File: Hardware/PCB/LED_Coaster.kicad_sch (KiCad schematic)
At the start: 88 parts, among them J1 Li-po, J3 USB_C_Receptacle_USB2.0_16P, J4 UART, Q1 AO3401A, SW1 SW_SPDT, U1 ESP32-C3-WROOM-02-H4, U3 MCP73871-2CC, U4 TLV75533PDBVR

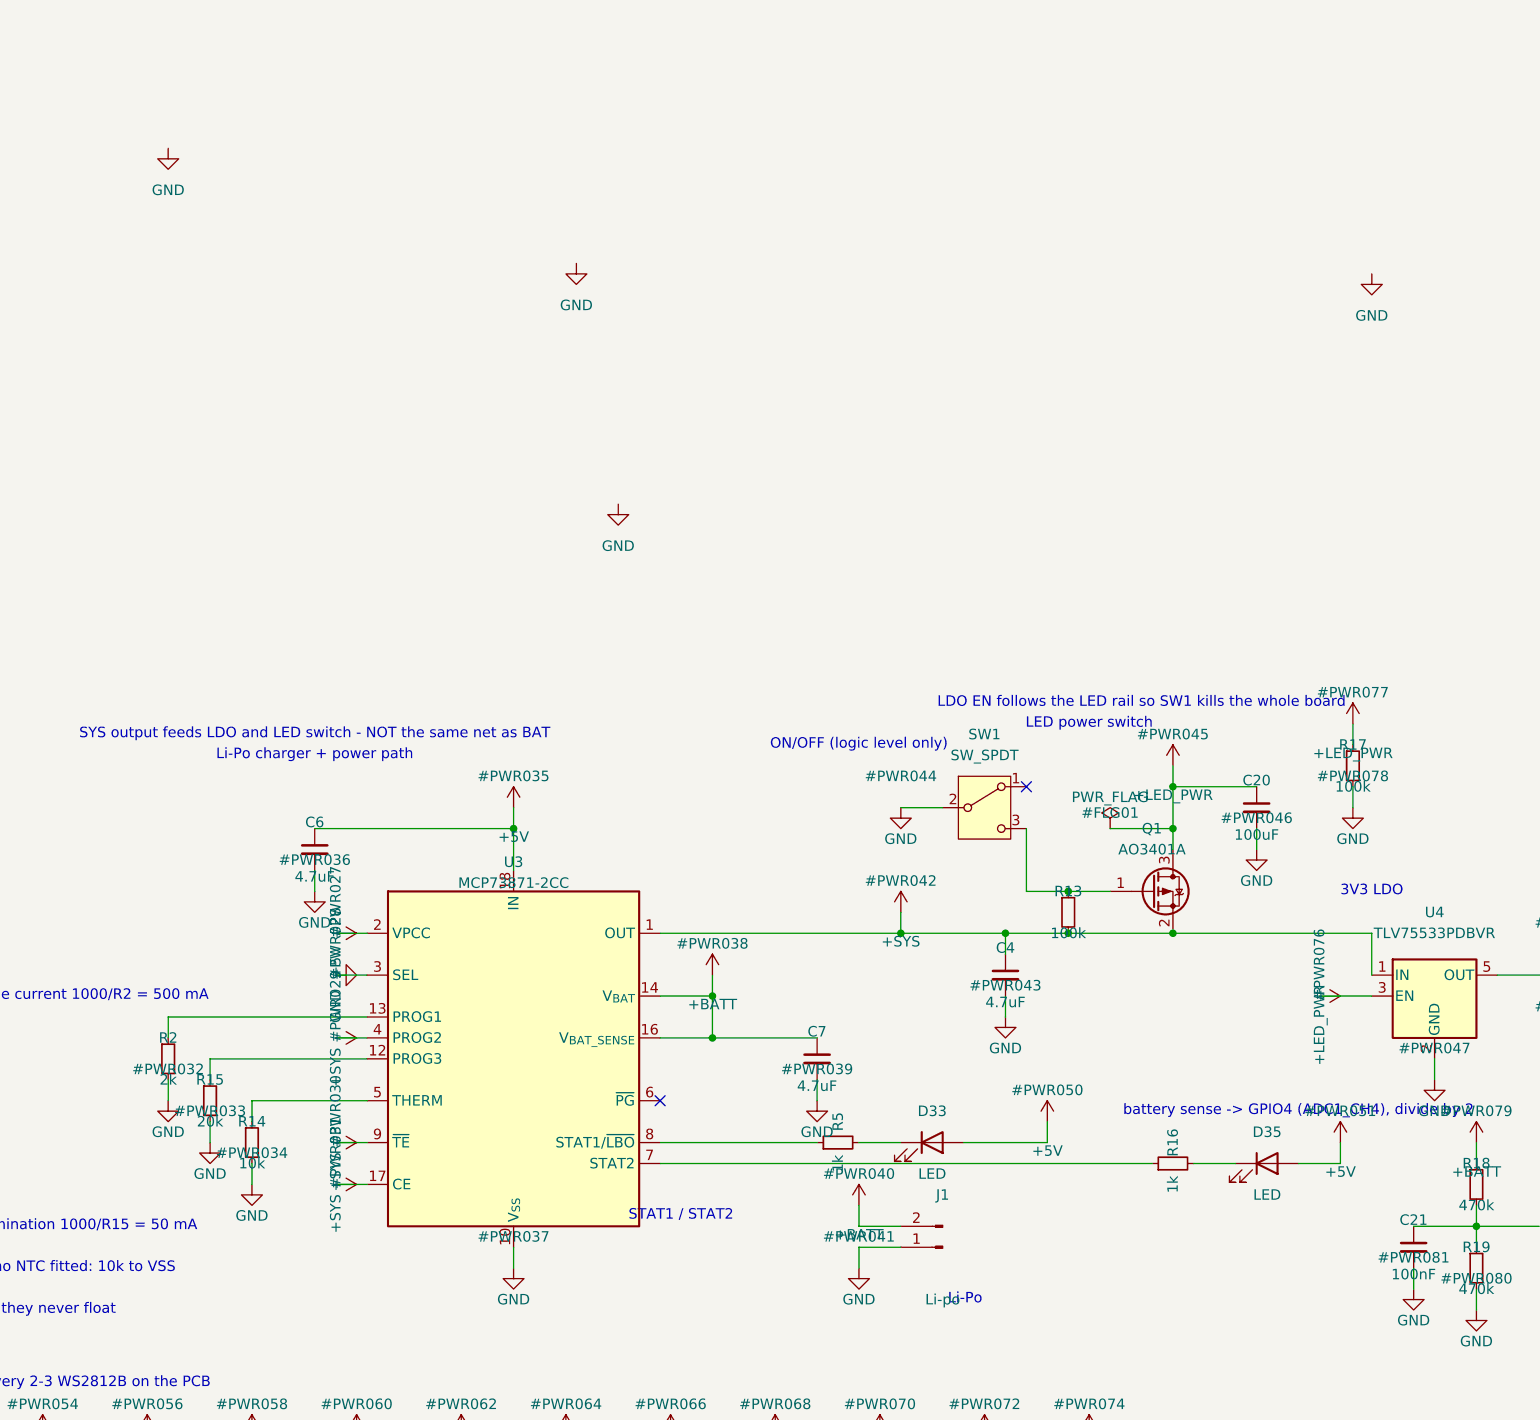
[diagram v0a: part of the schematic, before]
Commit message: Fix ERC errors: remove orphan GND symbols, add PWR_FLAG on +5V and GND
Six ERC errors, from two separate causes.

Four "pin not connected" errors: #PWR05, #PWR09, #PWR011 and #PWR016 were
GND symbols belonging to the old power section that my deletion pass failed
to remove, left floating with nothing attached.

Cause: those four use the GND_1..GND_5 library symbols, whose instances carry
a (lib_name ...) child. That pushes the (at x y rot) line from index 2 to
index 3 of the block, and the region filter read index 2 unconditionally, so
the position never parsed and the symbols were silently kept. 13 symbols in
the file have this shape; 4 of them fell inside the region being cleared.

Two "power pin not driven" errors on +5V (#PWR020) and GND (#PWR02) are
pre-existing, not from the rework. +5V is sourced by the USB-C VBUS pins and
GND by connector and module ground pins, none of which are power_out type, so
ERC has no evidence either rail is driven. Added PWR_FLAG on each, which is
the standard fix. +3V3, +BATT and +SYS were never flagged because the
regulator and charger outputs are real power_out pins, and +LED_PWR already
carries a PWR_FLAG from the earlier commit.

The netlist checker missed the orphans because its unconnected-pin test
skipped any reference starting with #PWR. It now audits every pin regardless
of prefix and reports singleton nets, plus checks that each power symbol
actually lands on a net with other pins on it. Both report clean.

Co-Authored-By: Claude Opus 5 <noreply@anthropic.com>
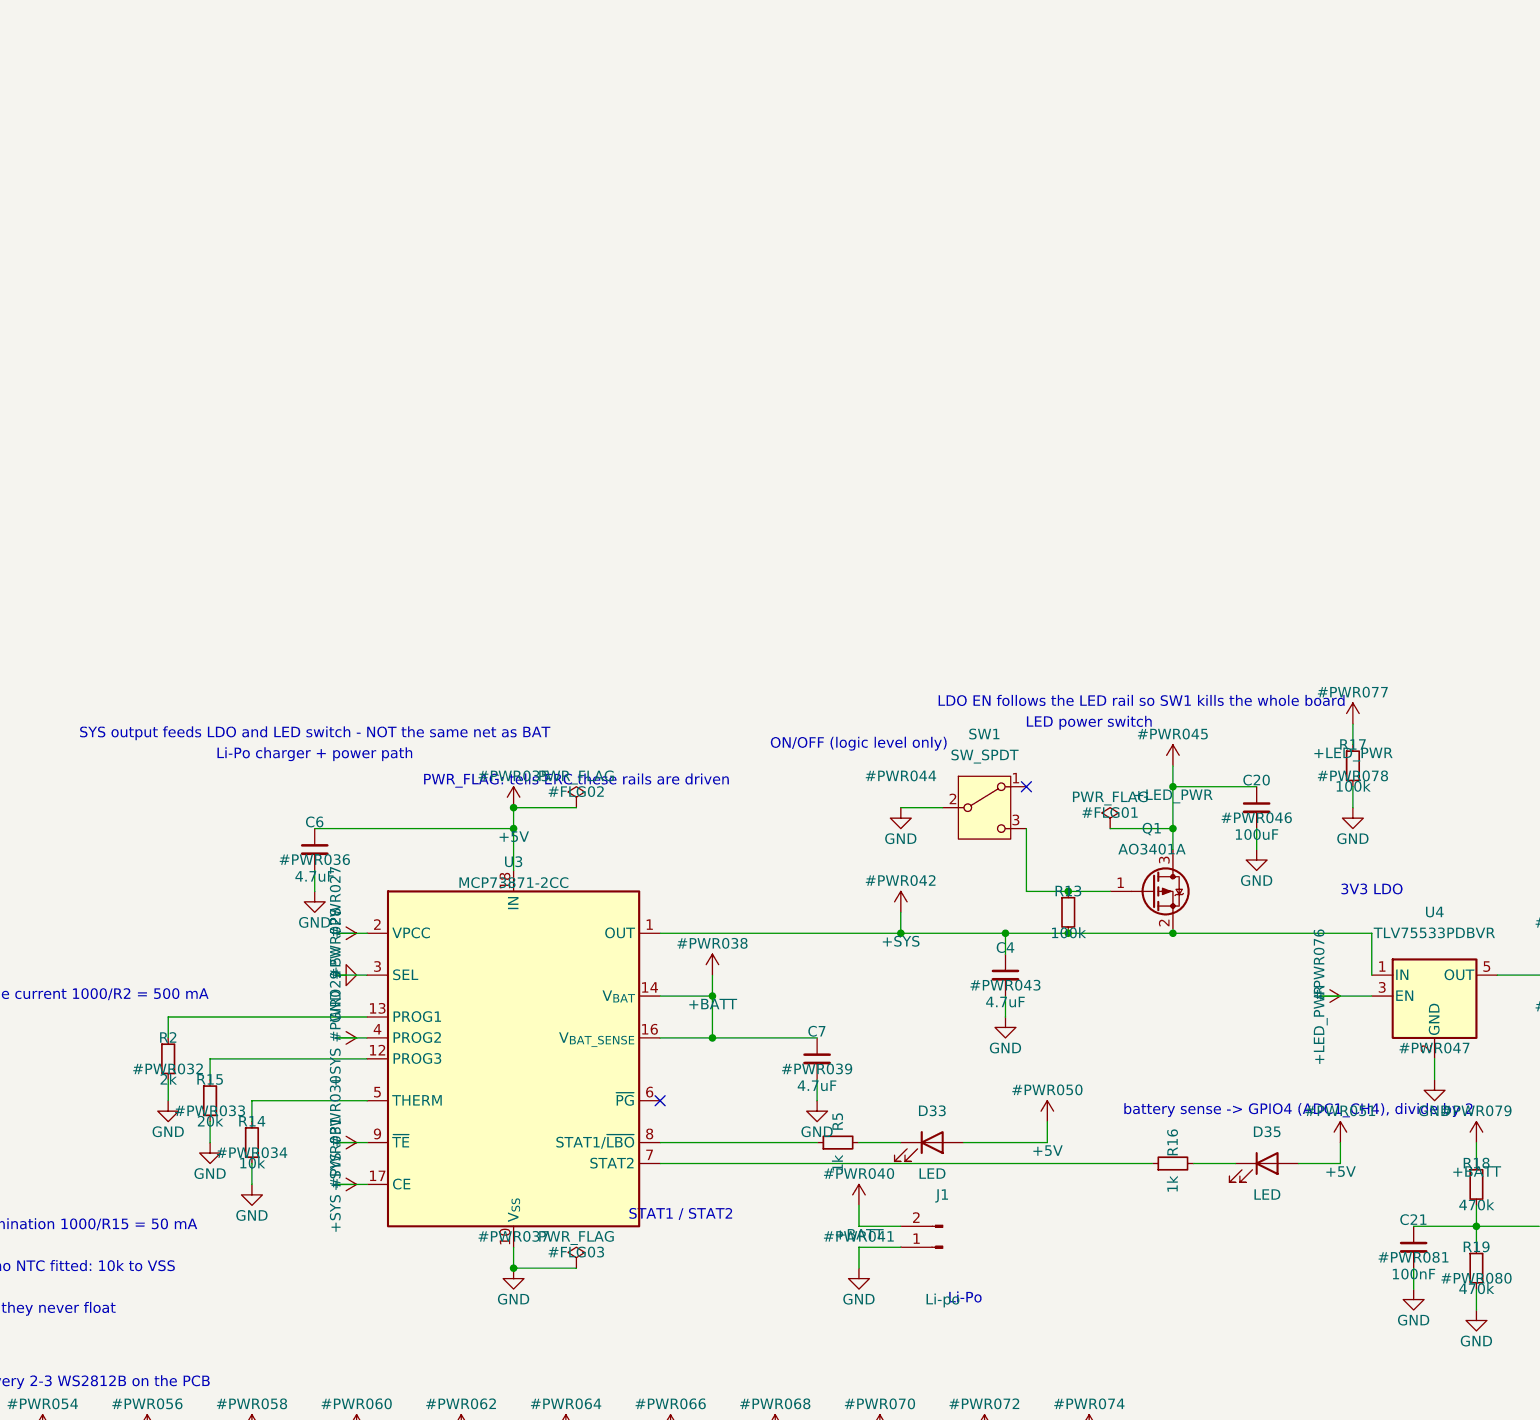
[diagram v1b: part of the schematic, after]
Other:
- note added: "PWR_FLAG: tells ERC these rails are driven"
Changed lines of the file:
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@@
 	)
 	(symbol
-		(lib_name "GND_2")
-		(lib_id "power:GND")
-		(at 422.91 172.72 0)
-		(mirror y)
-		(unit 1)
-		(exclude_from_sim no)
-		(in_bom yes)
-		(on_board yes)
-		(dnp no)
-		(fields_autoplaced yes)
-		(property "Reference" "#PWR016"
-			(at 422.91 179.07 0)
-			(effects
-				(font
-					(size 1.27 1.27)
-				)
-				(hide yes)
-			)
-		)
-		(property "Value" "GND"
-			(at 422.91 177.8 0)
-			(effects
-				(font
-					(size 1.27 1.27)
-				)
-			)
-		)
-		(property "Footprint" ""
-			(at 422.91 172.72 0)
-			(effects
-				(font
-					(size 1.27 1.27)
-				)
-				(hide yes)
-			)
-		)
-		(property "Datasheet" ""
-			(at 422.91 172.72 0)
-			(effects
-				(font
-					(size 1.27 1.27)
-				)
-				(hide yes)
-			)
-		)
-		(property "Description" "Power symbol creates a global label with name \"GND\" , ground"
-			(at 422.91 172.72 0)
-			(effects
-				(font
-					(size 1.27 1.27)
-				)
-				(hide yes)
-			)
-		)
-		(pin "1"
-		)
-		(instances
-			(project "LED_Coaster"
-				(path "/c3ec28d0-7d6a-45c7-8929-905948ef9c11"
-					(reference "#PWR016")
-					(unit 1)
-				)
-			)
-		)
-	)
-	(symbol
 		(lib_id "Switch:SW_SPST")
 		(at 227.33 198.12 0)
@@
 	)
 	(symbol
-		(lib_name "GND_2")
-		(lib_id "power:GND")
-		(at 514.35 144.78 0)
-		(unit 1)
-		(exclude_from_sim no)
-		(in_bom yes)
-		(on_board yes)
-		(dnp no)
-		(fields_autoplaced yes)
-		(property "Reference" "#PWR05"
-			(at 514.35 151.13 0)
-			(effects
-				(font
-					(size 1.27 1.27)
-				)
-				(hide yes)
-			)
-		)
-		(property "Value" "GND"
-			(at 514.35 149.86 0)
-			(effects
-				(font
-					(size 1.27 1.27)
-				)
-			)
-		)
-		(property "Footprint" ""
-			(at 514.35 144.78 0)
-			(effects
-				(font
-					(size 1.27 1.27)
-				)
-				(hide yes)
-			)
-		)
-		(property "Datasheet" ""
-			(at 514.35 144.78 0)
-			(effects
-				(font
-					(size 1.27 1.27)
-				)
-				(hide yes)
-			)
-		)
-		(property "Description" "Power symbol creates a global label with name \"GND\" , ground"
-			(at 514.35 144.78 0)
-			(effects
-				(font
-					(size 1.27 1.27)
-				)
-				(hide yes)
-			)
-		)
-		(pin "1"
-		)
-		(instances
-			(project "LED_Coaster"
-				(path "/c3ec28d0-7d6a-45c7-8929-905948ef9c11"
-					(reference "#PWR05")
-					(unit 1)
-				)
-			)
-		)
-	)
-	(symbol
 		(lib_name "GND_4")
 		(lib_id "power:GND")
@@
 	)
 	(symbol
-		(lib_name "GND_3")
-		(lib_id "power:GND")
-		(at 368.3 129.54 0)
-		(unit 1)
-		(exclude_from_sim no)
-		(in_bom yes)
-		(on_board yes)
-		(dnp no)
-		(fields_autoplaced yes)
-		(property "Reference" "#PWR09"
-			(at 368.3 135.89 0)
-			(effects
-				(font
-					(size 1.27 1.27)
-				)
-				(hide yes)
-			)
-		)
-		(property "Value" "GND"
-			(at 368.3 134.62 0)
-			(effects
-				(font
-					(size 1.27 1.27)
-				)
-			)
-		)
-		(property "Footprint" ""
-			(at 368.3 129.54 0)
-			(effects
-				(font
-					(size 1.27 1.27)
-				)
-				(hide yes)
-			)
-		)
-		(property "Datasheet" ""
-			(at 368.3 129.54 0)
-			(effects
-				(font
-					(size 1.27 1.27)
-				)
-				(hide yes)
-			)
-		)
-		(property "Description" "Power symbol creates a global label with name \"GND\" , ground"
-			(at 368.3 129.54 0)
-			(effects
-				(font
-					(size 1.27 1.27)
-				)
-				(hide yes)
-			)
-		)
-		(pin "1"
-		)
-		(instances
-			(project "LED_Coaster"
-				(path "/c3ec28d0-7d6a-45c7-8929-905948ef9c11"
-					(reference "#PWR09")
-					(unit 1)
-				)
-			)
-		)
-	)
-	(symbol
 		(lib_id "LED:WS2812B")
 		(at 162.56 58.42 0)
@@
 	)
 	(symbol
-		(lib_name "GND_3")
-		(lib_id "power:GND")
-		(at 417.83 143.51 0)
-		(unit 1)
-		(exclude_from_sim no)
-		(in_bom yes)
-		(on_board yes)
-		(dnp no)
-		(fields_autoplaced yes)
-		(property "Reference" "#PWR011"
-			(at 417.83 149.86 0)
-			(effects
-				(font
-					(size 1.27 1.27)
-				)
-				(hide yes)
-			)
-		)
-		(property "Value" "GND"
-			(at 417.83 148.59 0)
-			(effects
-				(font
-					(size 1.27 1.27)
-				)
-			)
-		)
-		(property "Footprint" ""
-			(at 417.83 143.51 0)
-			(effects
-				(font
-					(size 1.27 1.27)
-				)
-				(hide yes)
-			)
-		)
-		(property "Datasheet" ""
-			(at 417.83 143.51 0)
-			(effects
-				(font
-					(size 1.27 1.27)
-				)
-				(hide yes)
-			)
-		)
-		(property "Description" "Power symbol creates a global label with name \"GND\" , ground"
-			(at 417.83 143.51 0)
-			(effects
-				(font
-					(size 1.27 1.27)
-				)
-				(hide yes)
-			)
-		)
-		(pin "1"
-		)
-		(instances
-			(project "LED_Coaster"
-				(path "/c3ec28d0-7d6a-45c7-8929-905948ef9c11"
-					(reference "#PWR011")
-					(unit 1)
-				)
-			)
-		)
-	)
-	(symbol
 		(lib_id "power:+5V")
 		(at 132.08 247.65 0)
@@
 		(effects
 			(font
+				(size 1.27 1.27)
+			)
+		)
+	)
+	(wire
+		(pts
+			(xy 410.21 209.55) (xy 417.83 209.55)
+		)
+		(stroke
+			(width 0)
+			(type default)
+		)
+	)
+	(junction
+		(at 410.21 209.55)
+		(diameter 0)
+		(color 0 0 0 0)
+	)
+	(symbol
+		(lib_id "power:PWR_FLAG")
+		(at 417.83 209.55 0)
+		(unit 1)
+		(exclude_from_sim no)
+		(in_bom yes)
+		(on_board yes)
+		(dnp no)
+		(property "Reference" "#FLG02"
+			(at 417.83 207.645 0)
+			(effects
+				(font
+					(size 1.27 1.27)
+				)
+			)
+		)
+		(property "Value" "PWR_FLAG"
+			(at 417.83 205.74 0)
+			(effects
+				(font
+					(size 1.27 1.27)
+				)
+			)
+		)
+		(property "Footprint" ""
+			(at 417.83 209.55 0)
+			(effects
+				(font
+					(size 1.27 1.27)
+				)
+				(hide yes)
+			)
+		)
+		(property "Datasheet" "~"
+			(at 417.83 209.55 0)
+			(effects
+				(font
+					(size 1.27 1.27)
+				)
+				(hide yes)
+			)
+		)
+		(property "Description" "Special symbol for telling ERC where power comes from"
+			(at 417.83 209.55 0)
+			(effects
+				(font
+					(size 1.27 1.27)
+				)
+				(hide yes)
+			)
+		)
+		(pin "1"
+		)
+		(instances
+			(project "LED_Coaster"
+				(path "/c3ec28d0-7d6a-45c7-8929-905948ef9c11"
+					(reference "#FLG02")
+					(unit 1)
+				)
+			)
+		)
+	)
+	(wire
+		(pts
+			(xy 410.21 265.43) (xy 417.83 265.43)
+		)
+		(stroke
+			(width 0)
+			(type default)
+		)
+	)
+	(junction
+		(at 410.21 265.43)
+		(diameter 0)
+		(color 0 0 0 0)
+	)
+	(symbol
+		(lib_id "power:PWR_FLAG")
+		(at 417.83 265.43 0)
+		(unit 1)
+		(exclude_from_sim no)
+		(in_bom yes)
+		(on_board yes)
+		(dnp no)
+		(property "Reference" "#FLG03"
+			(at 417.83 263.525 0)
+			(effects
+				(font
+					(size 1.27 1.27)
+				)
+			)
+		)
+		(property "Value" "PWR_FLAG"
+			(at 417.83 261.62 0)
+			(effects
+				(font
+					(size 1.27 1.27)
+				)
+			)
+		)
+		(property "Footprint" ""
+			(at 417.83 265.43 0)
+			(effects
+				(font
+					(size 1.27 1.27)
+				)
+				(hide yes)
+			)
+		)
+		(property "Datasheet" "~"
+			(at 417.83 265.43 0)
+			(effects
+				(font
+					(size 1.27 1.27)
+				)
+				(hide yes)
+			)
+		)
+		(property "Description" "Special symbol for telling ERC where power comes from"
+			(at 417.83 265.43 0)
+			(effects
+				(font
+					(size 1.27 1.27)
+				)
+				(hide yes)
+			)
+		)
+		(pin "1"
+		)
+		(instances
+			(project "LED_Coaster"
+				(path "/c3ec28d0-7d6a-45c7-8929-905948ef9c11"
+					(reference "#FLG03")
+					(unit 1)
+				)
+			)
+		)
+	)
+	(text "PWR_FLAG: tells ERC these rails are driven"
+		(exclude_from_sim no)
+		(at 417.83 206.38 0)
+		(effects
+			(font

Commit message: Set verified LCSC part numbers; correct the charger to the 4.20V variant
The charger part number was wrong. C637761, carried over from the original
fix spec as "MCP73871-2CCI/ML", is actually MCP73871-4CAI/ML. Per the
datasheet's Product Identification System the leading digit selects the
charge voltage: 2CC is 4.20V, 4CA is 4.40V. Fitting it would have regulated
a standard 4.2V Li-Po cell to 4.40V - an overcharge, with the cell life and
safety consequences that implies. It was also out of stock, which is what
prompted the search that caught it.

U3 MPN is now C5121473 = MCP73871-2CCI/ML = 4.20V, the variant the design was
actually built around. Its CC suffix also enables LBO at 3.1V, so STAT1
doubles as a low-battery indicator.

Part numbers filled in, all verified against their manufacturer part number
rather than taken on trust:

  R13, R17  100k 0805   C149504   0805W8F1003T5E
  R15       20k 0805    C4328     0805W8F2002T5E  (2002 = 200 x 10^2 = 20k)
  R18, R19  470k 0805   C17709    0805W8F4703T5E
  C20       22uF 0805   C296305   YAGEO 22uF 6.3V X5R

C20 dropped from 100uF 1210 to 22uF 0805: the 100uF part carried a 66-piece
minimum order, which does not suit a 5-board run, and the capacitance is not
needed. Low-frequency droop is set by battery ESR plus the charger's ~200 mOhm
BAT-to-SYS path plus the FET - roughly 400 mOhm - so a 1 A step drops ~400 mV
regardless of the bulk cap. The cap's real job is supplying fast edges, and
22 uF alongside the twelve distributed 100nF covers that comfortably.

C21 relabelled 100nF -> 0.1uF so it merges with C2 onto a single BOM line;
same physical part, C28233.

Netlist and structure re-verified: 0 malformed forms, no orphan pins, no
duplicate references, BAT_SENSE still reaches U1 GPIO4.

Co-Authored-By: Claude Opus 5 <noreply@anthropic.com>
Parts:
- C20: value 100uF -> 22uF; footprint Capacitor_SMD:C_1210_3225Metric_Pad1.33x2.70mm_HandSolder -> Capacitor_SMD:C_0805_2012Metric_Pad1.18x1.45mm_HandSolder; MPN (none) -> C296305
- C21: value 100nF -> 0.1uF
- R13, R17: MPN (none) -> C149504
- R15: MPN (none) -> C4328
- R18, R19: MPN (none) -> C17709
- U3: MPN C637761 -> C5121473
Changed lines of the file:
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@@
 			)
 		)
-		(property "MPN" "C637761"
+		(property "MPN" "C5121473"
 			(at 410.21 240.03 0)
 			(hide yes)
@@
 			)
 		)
-		(property "MPN" ""
+		(property "MPN" "C4328"
 			(at 373.38 245.11 0)
 			(hide yes)
@@
 			)
 		)
-		(property "MPN" ""
+		(property "MPN" "C149504"
 			(at 477.52 222.25 0)
 			(hide yes)
@@
 			)
 		)
-		(property "Value" "100uF"
+		(property "Value" "22uF"
 			(at 500.38 212.852 0)
 			(show_name no)
@@
 			)
 		)
-		(property "Footprint" "Capacitor_SMD:C_1210_3225Metric_Pad1.33x2.70mm_HandSolder"
+		(property "Footprint" "Capacitor_SMD:C_0805_2012Metric_Pad1.18x1.45mm_HandSolder"
 			(at 500.38 209.55 0)
 			(hide yes)
@@
 			)
 		)
-		(property "MPN" ""
+		(property "MPN" "C296305"
 			(at 500.38 209.55 0)
 			(hide yes)
@@
 			)
 		)
-		(property "MPN" ""
+		(property "MPN" "C149504"
 			(at 511.81 204.47 0)
 			(hide yes)
@@
 			)
 		)
-		(property "MPN" ""
+		(property "MPN" "C17709"
 			(at 527.05 255.27 0)
 			(hide yes)
@@
 			)
 		)
-		(property "MPN" ""
+		(property "MPN" "C17709"
 			(at 527.05 265.43 0)
 			(hide yes)
@@
 			)
 		)
-		(property "Value" "100nF"
+		(property "Value" "0.1uF"
 			(at 519.43 266.192 0)
 			(show_name no)
